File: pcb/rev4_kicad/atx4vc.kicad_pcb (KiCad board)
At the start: 2 copper layers, 69 x 69 mm, 51 parts, among them IC1 MY_7905DT, IC2 MAX486X/SOT, J1 USB_C16PIN, J2 ATX24RH, SW1 SPST_TACT-EVQQ2

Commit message: adjusted power mode silkscreen
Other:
- board text added: "HARD"
- board text added: "PWR MODE"
- board text added: "SOFT"
- board text removed: "HARD PWR"
- board text removed: "SOFT PWR"
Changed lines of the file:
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@@
 		)
 	)
-	(gr_text "SOFT\nPWR"
-		(at 136.25 129.5 0)
+	(gr_text "SOFT"
+		(at 136.25 130.5 0)
 		(layer "F.SilkS")
 		(effects
@@
 		)
 	)
-	(gr_text "HARD\nPWR"
-		(at 143.25 129.5 0)
+	(gr_text "PWR\nMODE"
+		(at 132.5 123 0)
 		(layer "F.SilkS")
 		(effects
+			(font
+				(size 1.25 1.25)
+				(thickness 0.1875)
+			)
+			(justify left)
+		)
+	)
+	(gr_text "HARD"
+		(at 143.25 130.5 0)
+		(layer "F.SilkS")
+		(effects

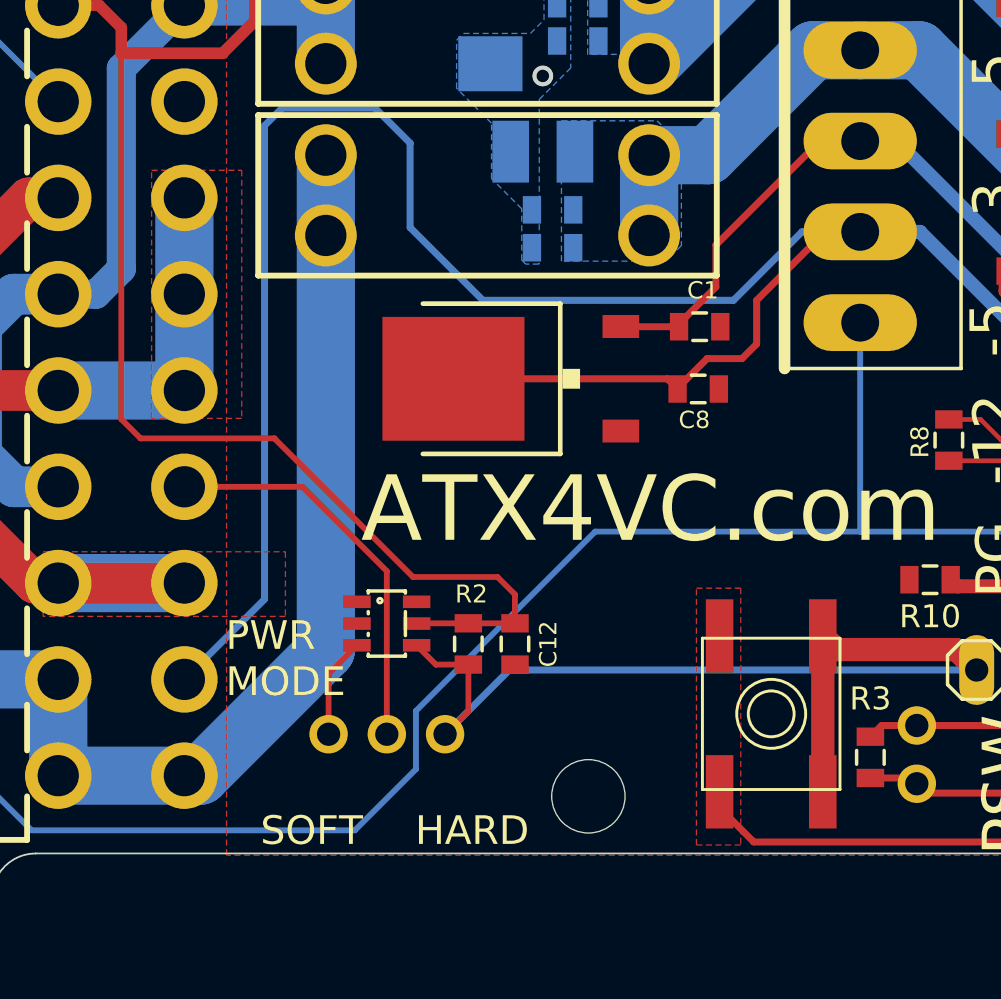
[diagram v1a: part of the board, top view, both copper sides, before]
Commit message: adjust silkscreen
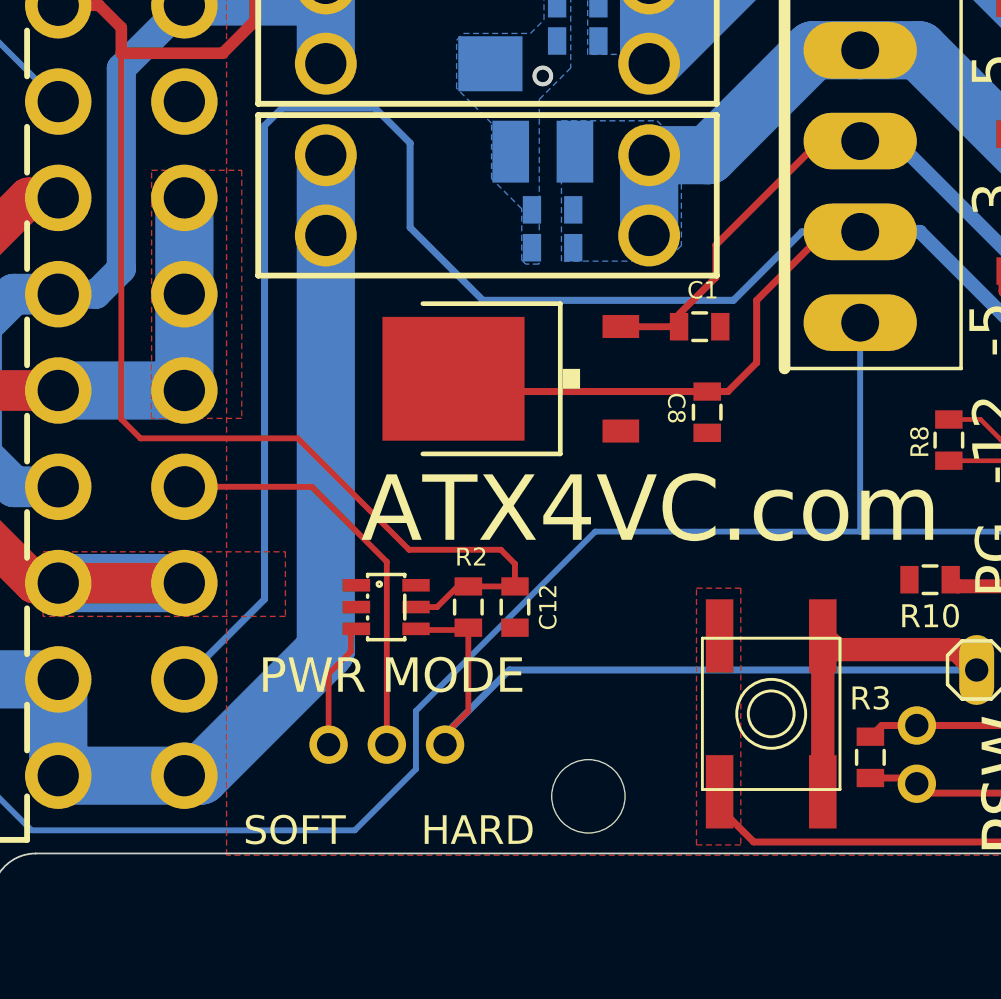
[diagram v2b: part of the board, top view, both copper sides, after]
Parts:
- moved C12 1.61 mm to (145.1, 120.8)
- moved R2 1.61 mm to (143.1, 120.8)
- moved C8 1.08 mm to (153.5, 112.2), turned to 90 degrees
- moved IC2 0.72 mm to (139.5, 120.8)
- moved JP7 0.45 mm to (139.5, 126.8)
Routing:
- net Net-(IC2-KEY): track 44.5 -> 46.8 mm
- net Net-(IC2-OUTL): track 4.39 -> 5.55 mm
- net Net-(J2-PS_ON): track 17.5 -> 18.2 mm
- net Net-(IC1-VI): track 114.7 -> 115.3 mm
